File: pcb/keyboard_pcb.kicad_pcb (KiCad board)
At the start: 2 copper layers, 142.9 x 98.6 mm, 26 parts, among them J1 TRRS, K00 KEYSW, K01 KEYSW, K02 KEYSW, K03 KEYSW, K04 KEYSW, K05 KEYSW, K10 KEYSW, K11 KEYSW, K12 KEYSW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

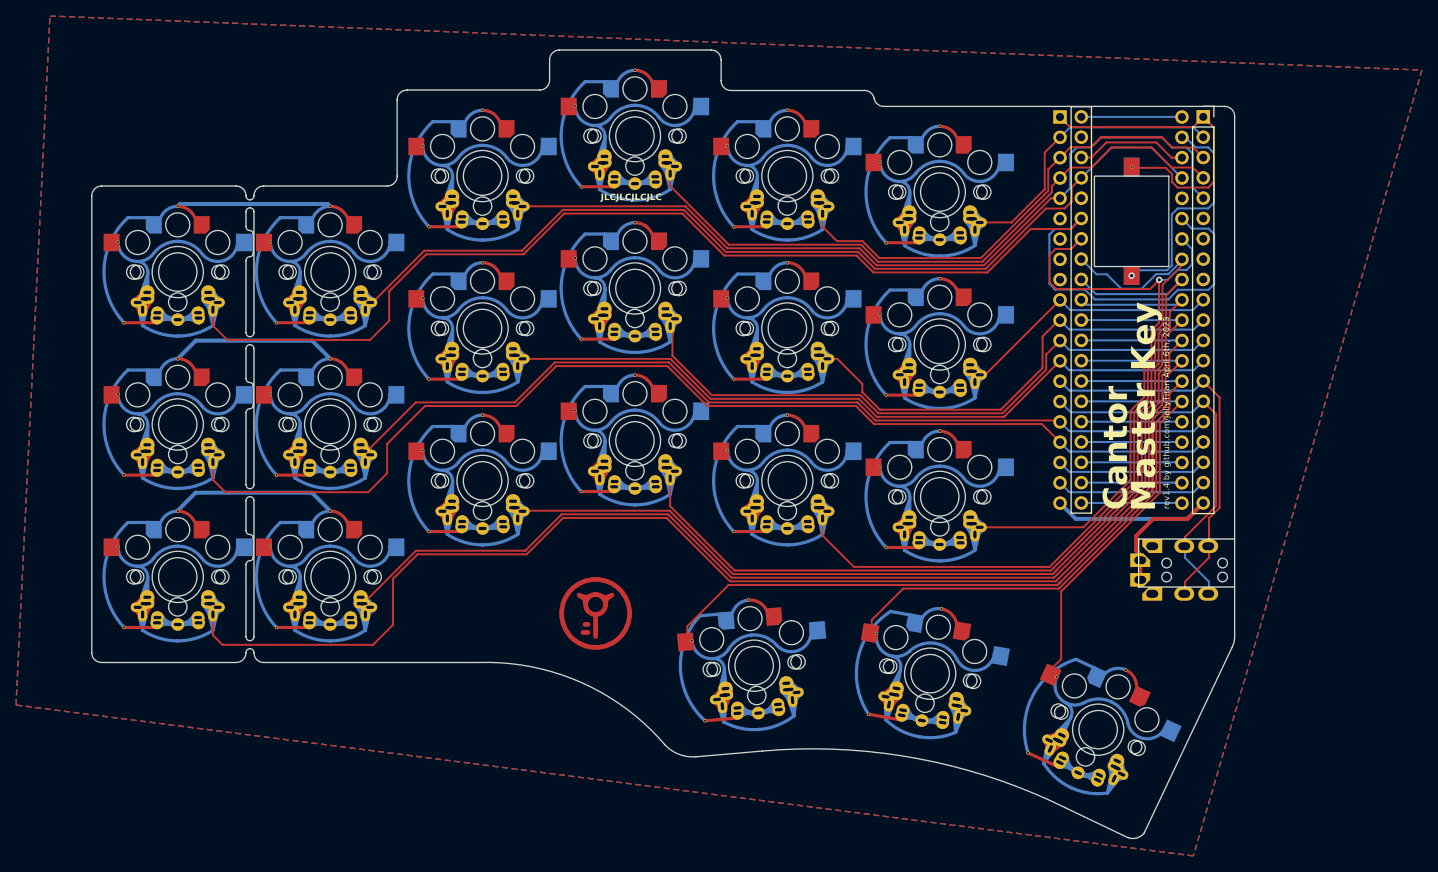
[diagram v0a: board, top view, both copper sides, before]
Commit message: Fixed choc 2nd min misalingment Revised 'everything' footprint: combined red-dragon and MX hole removed organic masks in leiu of exotic annular rings fixed malformed edge shapes
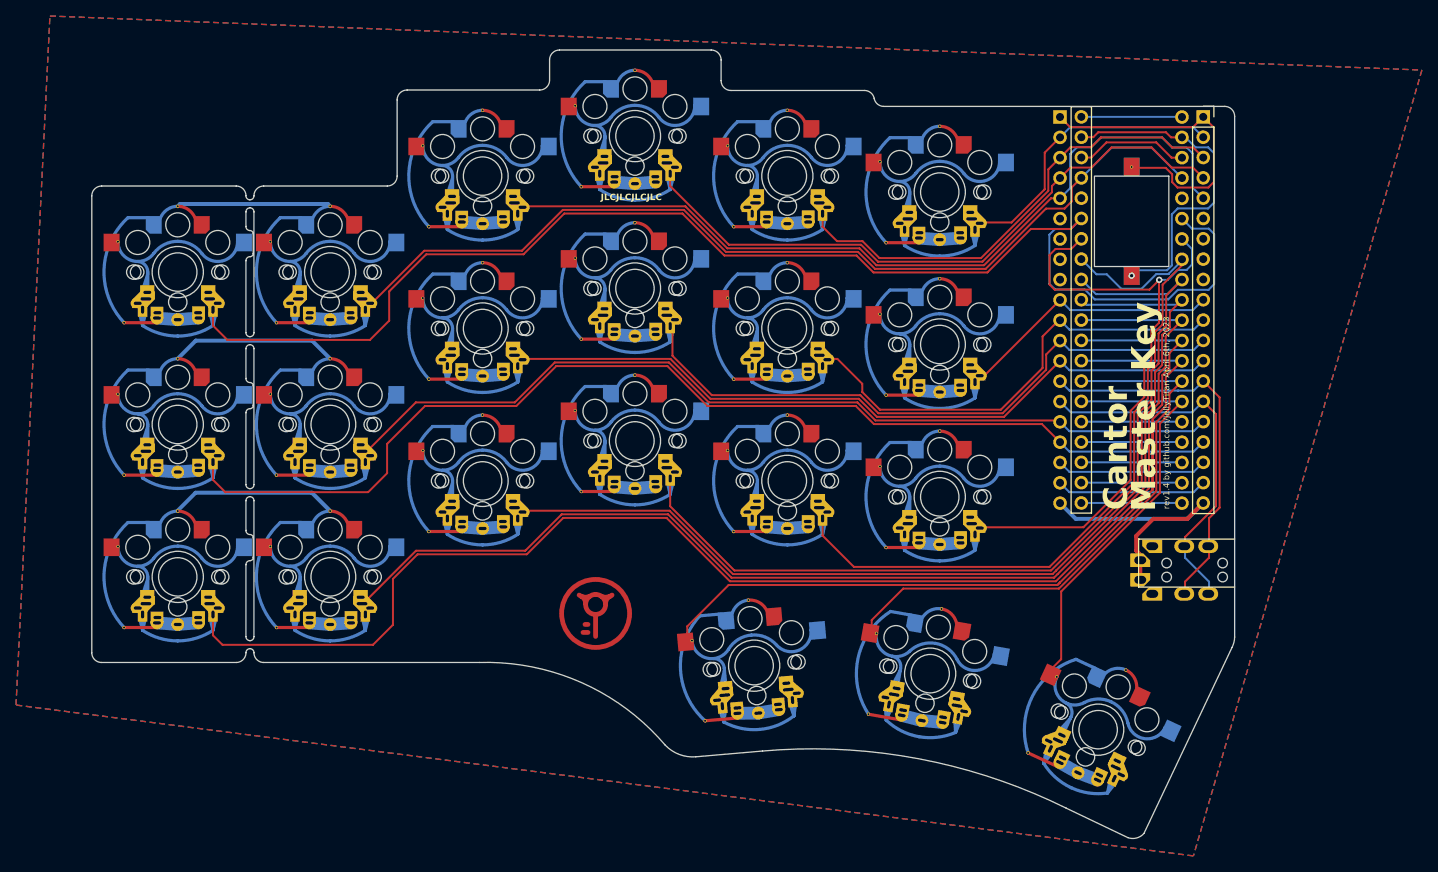
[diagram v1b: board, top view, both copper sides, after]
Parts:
- K00, K01, K02, K03, K04, K05, K10, K11, K12, K13, K14, K15, K20, K21, K22, K23, K24, K25, K30, K31, K32: footprint Cantor_MasterKey:ALL LOWs CANTOR -> Cantor_MasterKey:ALL LOWs CANTOR v4.1
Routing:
- net GND: track 108.9 -> 122.0 mm

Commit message: Updated docs and fixed footprint mask
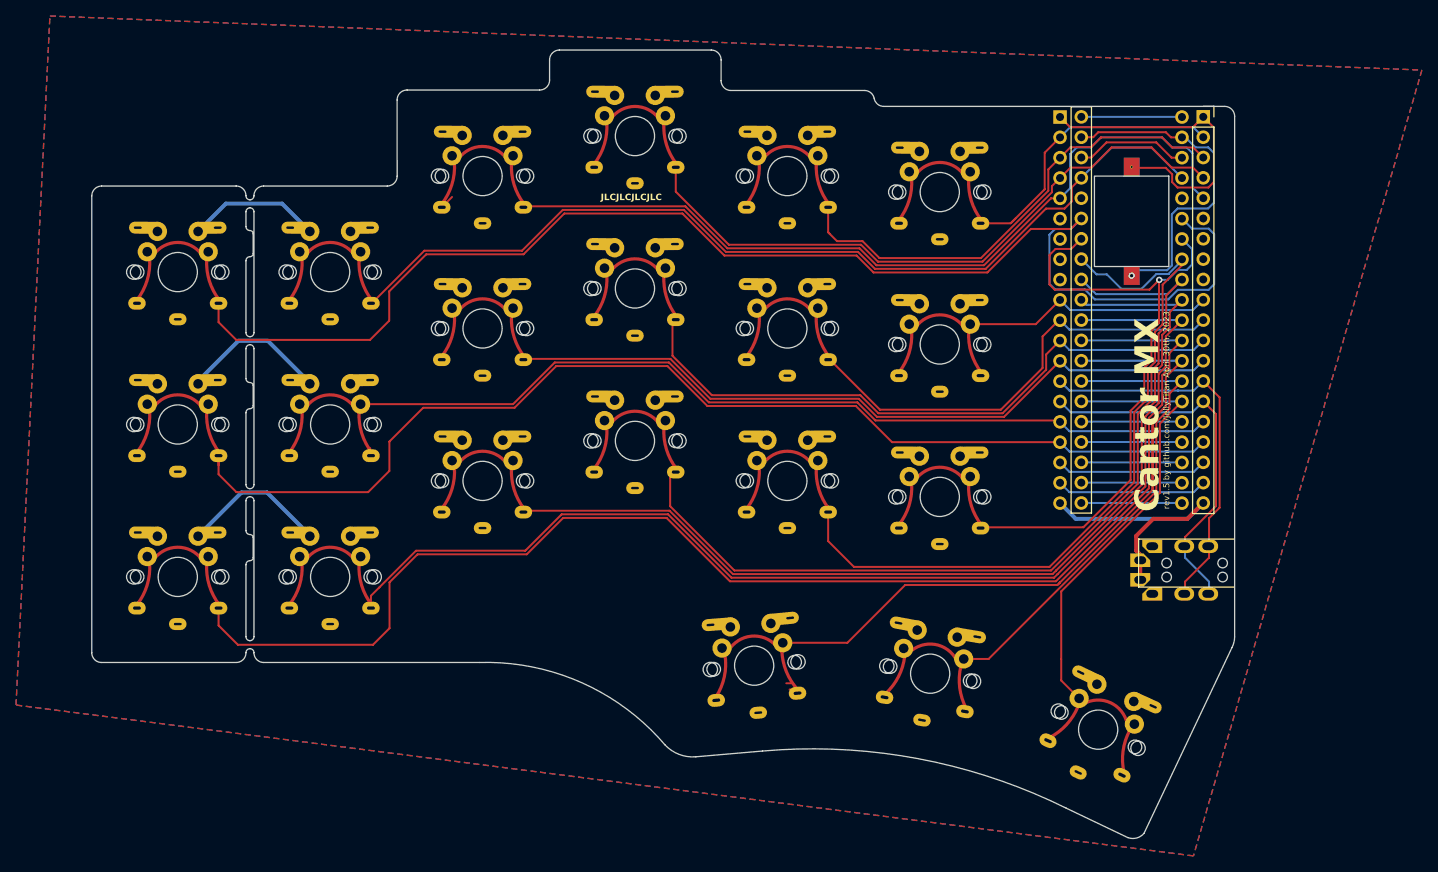
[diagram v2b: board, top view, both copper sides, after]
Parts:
- removed REF**: CANTOR MASTER KEY LOGO_UNDERSKIN, Cantor_MasterKey:CANTOR MASTER KEY LOGO_UNDERSKIN
- removed REF**: CANTOR MASTER KEY LOGO SILKS, Cantor_MasterKey:CANTOR MASTER KEY LOGO SILKS
- K00, K01, K02, K03, K04, K05, K10, K11, K12, K13, K14, K15, K20, K21, K22, K23, K24, K25, K30, K31, K32: footprint Cantor_MasterKey:ALL LOWs CANTOR v4.1 -> Cantor_MasterKey:CherryMX_ChocV2_1u_DS
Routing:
- net /k30: track 108.6 -> 95.5 mm
- net /k31: track 71.5 -> 60.4 mm
- net GND: track 122.0 -> 114.4 mm
- net /k32: track 54.1 -> 57.4 mm
- net /k23: track 111.9 -> 113.0 mm
- net /k11: track 113.6 -> 112.6 mm
- net /k10: track 140.2 -> 141.1 mm
- net /k15: track 32.9 -> 32.1 mm
- net /k14: track 58.1 -> 57.4 mm
- net /k05: track 36.1 -> 36.8 mm
- net /k20: track 170.9 -> 170.2 mm
- net /k04: track 59.7 -> 60.2 mm
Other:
- board text added: "Cantor MX"
- board text added: "Rev 1.4: * Cherry MX * Kailh Choc V1 * Kailh Choc V2"
- board text added: "rev1.5 by github.com/JellyTitan April 30th, 2023"
- board text removed: "Cantor"
- board text removed: "Master Key"
- board text removed: "Rev 1.3: * Cherry MX 5pin * Cherry MXLP * Kailh Choc V1 * Kailh Choc V2 * Choc Hotswops * Gateron LP * TTC KS32 * Red Dragon LP"
- board text removed: "rev1.4 by github.com/JellyTitan April 6th, 2023"

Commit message: Footprint cleanup reverted branding to older MX specific style
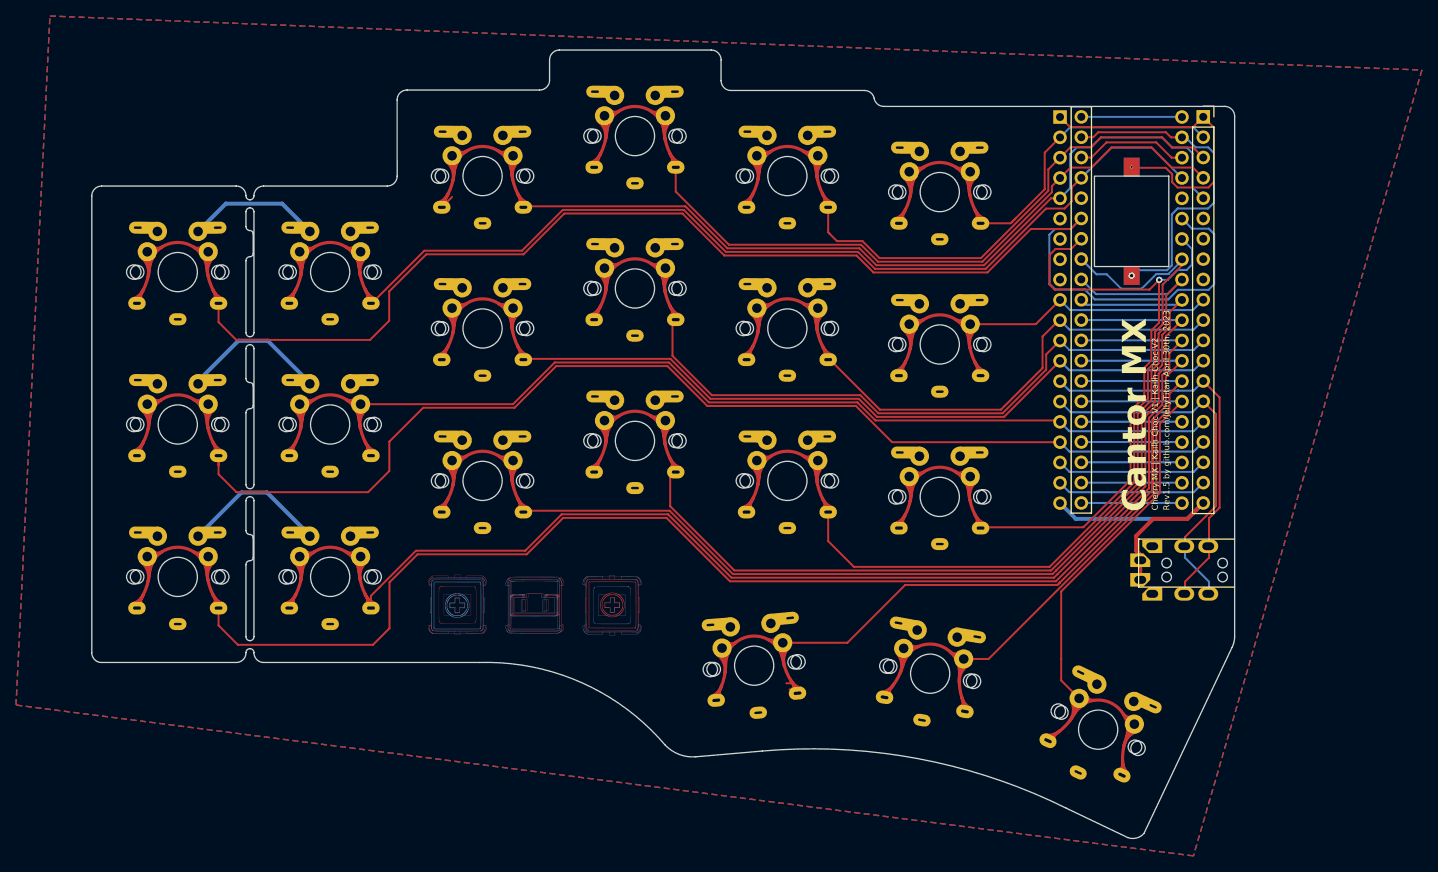
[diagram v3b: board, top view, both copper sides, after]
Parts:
- added G***: Cantor MX logo 3-switches top, Cantor_MasterKey:Cantor MX logo 3-switches top, F.Cu at (113.2, 111.5)
- added G***: Cantor MX logo 3-switches ortho, Cantor_MasterKey:Cantor MX logo 3-switches ortho, B.Cu at (188.9, 85.1)
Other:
- board text added: "Cantor MX rev1.5 by JellyTitan"
- board text added: "Cherry MX | Kailh Choc V1 | Kailh Choc V2"
- board text added: "Rev1.5 by github.com/JellyTitan April 30th, 2023"
- board text removed: "Cantor Master Key"
- board text removed: "Rev 1.4: * Cherry MX * Kailh Choc V1 * Kailh Choc V2"
- board text removed: "rev1.5 by github.com/JellyTitan April 30th, 2023"

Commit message: Fixed trrs footprint added key numbering cleaned up wiring between blackpill holes
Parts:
- J1: footprint Cantor_MasterKey:MJ-4PP-9_CANTOR_KITCHEN_SINK -> Cantor_MasterKey:MJ-4PP-9_Cantor_MX_TX-RX_Crossover
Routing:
- net /k22: track 125.0 -> 122.9 mm
- net GND: track 114.4 -> 113.0 mm, vias 1 -> 0
- net /k30: track 95.5 -> 94.3 mm
- net /k05: track 36.8 -> 36.0 mm
- net /k15: track 32.1 -> 31.4 mm
- net /k32: track 57.4 -> 56.8 mm
- net /k13: track 79.9 -> 79.4 mm
